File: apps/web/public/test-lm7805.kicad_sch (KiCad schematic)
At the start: 5 parts, among them J1 VIN_CONN, J2 VOUT_5V, U1 LM7805

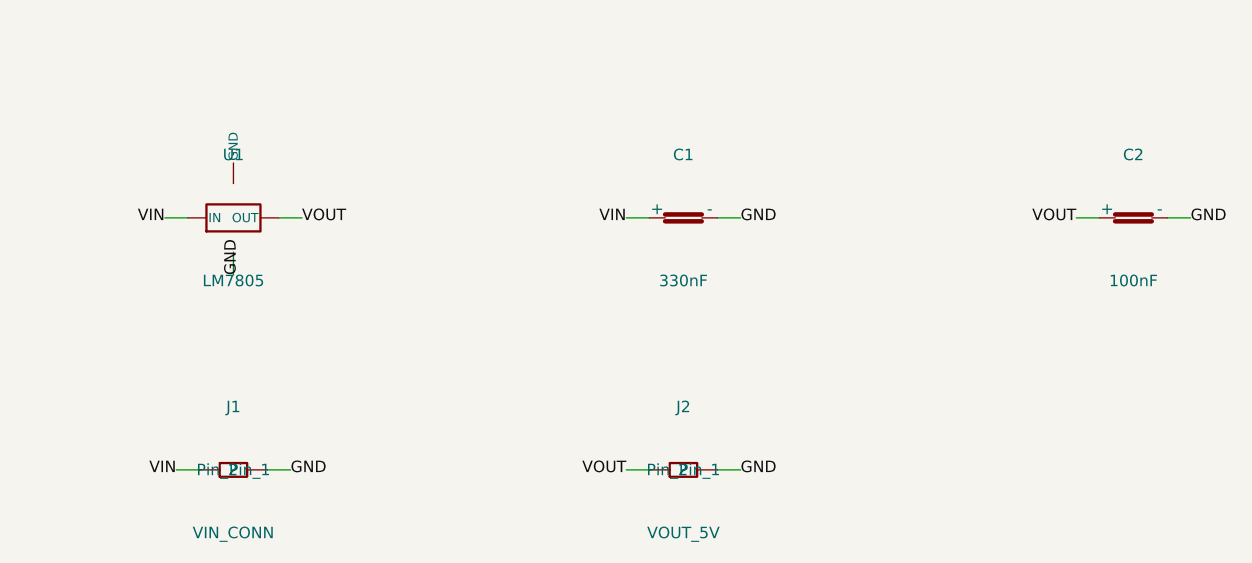
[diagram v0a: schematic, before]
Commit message: feat(kicad): Timer:NE555P named pins + compact paper for better zoom
- Add Timer:NE555P inline symbol with proper named pins:
  GND(1) TRIG(2) OUT(3) RST(4) CTRL(5) THR(6) DIS(7) VCC(8)
- _simple_lib_id: detect NE555/LM555/NA555/TLC555/ICM7555 → Timer:NE555P
- _pin_offset: Timer:NE555P reuses DIP-8 _IC_PIN_OFFSETS geometry
- Reduce paper margins 20→8mm, col_step 50→45, row_step 28→25
  LM7805 paper: 165x88 → 128x59mm (-40%) = composants 40% plus grands
  au zoom-to-fit KiCanvas
- Regenerate 3 fixtures (lm7805/ne555/esp32)
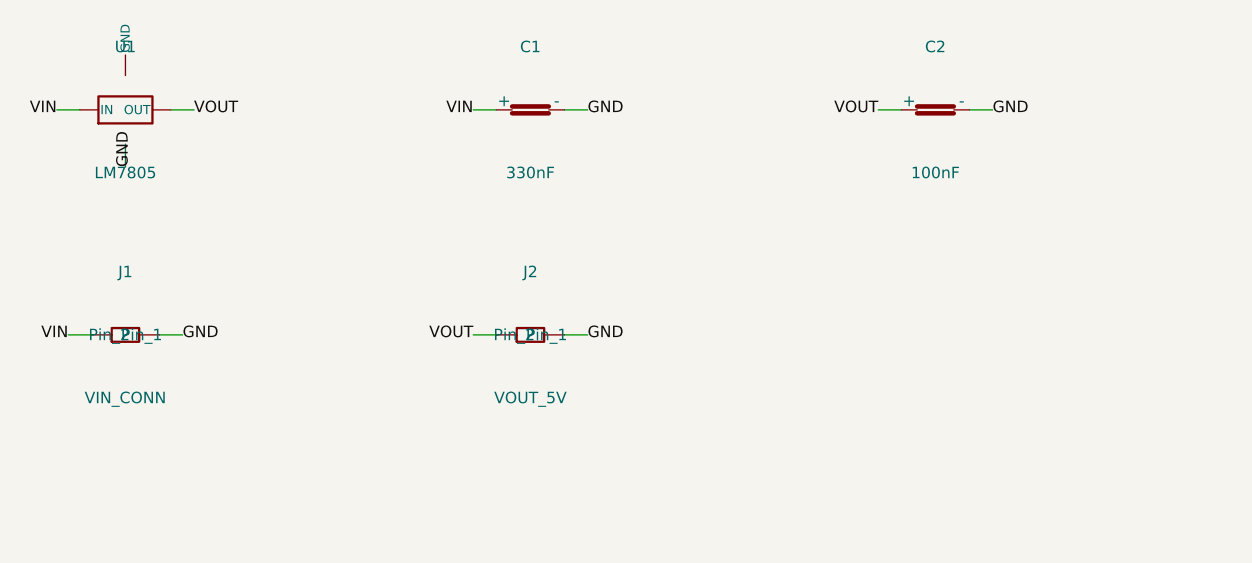
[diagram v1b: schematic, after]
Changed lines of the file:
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@@
 (kicad_sch (version 20230121) (generator "layrix-circuit-synth")
-  (paper "User" 165 88)
-  (symbol (lib_id "Device:VReg_3Pin") (at 20 20 0) (unit 1) (in_bom yes) (on_board yes)
-    (property "Reference" "U1" (at 20 13 0) (effects (font (size 1.27 1.27)) (justify center)))
-    (property "Value" "LM7805" (at 20 27 0) (effects (font (size 1.27 1.27)) (justify center)))
-    (property "Footprint" "Package_TO_SOT_THT:TO-220-3_Vertical" (at 20 30 0) (effects (font (size 1.27 1.27)) (hide yes)))
+  (paper "User" 128 59)
+  (symbol (lib_id "Device:VReg_3Pin") (at 8 8 0) (unit 1) (in_bom yes) (on_board yes)
+    (property "Reference" "U1" (at 8 1 0) (effects (font (size 1.27 1.27)) (justify center)))
+    (property "Value" "LM7805" (at 8 15 0) (effects (font (size 1.27 1.27)) (justify center)))
+    (property "Footprint" "Package_TO_SOT_THT:TO-220-3_Vertical" (at 8 18 0) (effects (font (size 1.27 1.27)) (hide yes)))
   )
-  (symbol (lib_id "Device:C") (at 70 20 0) (unit 1) (in_bom yes) (on_board yes)
-    (property "Reference" "C1" (at 70 13 0) (effects (font (size 1.27 1.27)) (justify center)))
-    (property "Value" "330nF" (at 70 27 0) (effects (font (size 1.27 1.27)) (justify center)))
-    (property "Footprint" "Capacitor_THT:C_Disc_D5.0mm_W2.5mm_P5.00mm" (at 70 30 0) (effects (font (size 1.27 1.27)) (hide yes)))
+  (symbol (lib_id "Device:C") (at 53 8 0) (unit 1) (in_bom yes) (on_board yes)
+    (property "Reference" "C1" (at 53 1 0) (effects (font (size 1.27 1.27)) (justify center)))
+    (property "Value" "330nF" (at 53 15 0) (effects (font (size 1.27 1.27)) (justify center)))
+    (property "Footprint" "Capacitor_THT:C_Disc_D5.0mm_W2.5mm_P5.00mm" (at 53 18 0) (effects (font (size 1.27 1.27)) (hide yes)))
   )
-  (symbol (lib_id "Device:C") (at 120 20 0) (unit 1) (in_bom yes) (on_board yes)
-    (property "Reference" "C2" (at 120 13 0) (effects (font (size 1.27 1.27)) (justify center)))
-    (property "Value" "100nF" (at 120 27 0) (effects (font (size 1.27 1.27)) (justify center)))
-    (property "Footprint" "Capacitor_THT:C_Disc_D5.0mm_W2.5mm_P5.00mm" (at 120 30 0) (effects (font (size 1.27 1.27)) (hide yes)))
+  (symbol (lib_id "Device:C") (at 98 8 0) (unit 1) (in_bom yes) (on_board yes)
+    (property "Reference" "C2" (at 98 1 0) (effects (font (size 1.27 1.27)) (justify center)))
+    (property "Value" "100nF" (at 98 15 0) (effects (font (size 1.27 1.27)) (justify center)))
+    (property "Footprint" "Capacitor_THT:C_Disc_D5.0mm_W2.5mm_P5.00mm" (at 98 18 0) (effects (font (size 1.27 1.27)) (hide yes)))
   )
-  (symbol (lib_id "Connector_Generic:Conn_01x02") (at 20 48 0) (unit 1) (in_bom yes) (on_board yes)
-    (property "Reference" "J1" (at 20 41 0) (effects (font (size 1.27 1.27)) (justify center)))
-    (property "Value" "VIN_CONN" (at 20 55 0) (effects (font (size 1.27 1.27)) (justify center)))
-    (property "Footprint" "Connector_PinHeader_2.54mm:PinHeader_1x02_P2.54mm_Vertical" (at 20 58 0) (effects (font (size 1.27 1.27)) (hide yes)))
+  (symbol (lib_id "Connector_Generic:Conn_01x02") (at 8 33 0) (unit 1) (in_bom yes) (on_board yes)
+    (property "Reference" "J1" (at 8 26 0) (effects (font (size 1.27 1.27)) (justify center)))
+    (property "Value" "VIN_CONN" (at 8 40 0) (effects (font (size 1.27 1.27)) (justify center)))
+    (property "Footprint" "Connector_PinHeader_2.54mm:PinHeader_1x02_P2.54mm_Vertical" (at 8 43 0) (effects (font (size 1.27 1.27)) (hide yes)))
   )
-  (symbol (lib_id "Connector_Generic:Conn_01x02") (at 70 48 0) (unit 1) (in_bom yes) (on_board yes)
-    (property "Reference" "J2" (at 70 41 0) (effects (font (size 1.27 1.27)) (justify center)))
-    (property "Value" "VOUT_5V" (at 70 55 0) (effects (font (size 1.27 1.27)) (justify center)))
-    (property "Footprint" "Connector_PinHeader_2.54mm:PinHeader_1x02_P2.54mm_Vertical" (at 70 58 0) (effects (font (size 1.27 1.27)) (hide yes)))
+  (symbol (lib_id "Connector_Generic:Conn_01x02") (at 53 33 0) (unit 1) (in_bom yes) (on_board yes)
+    (property "Reference" "J2" (at 53 26 0) (effects (font (size 1.27 1.27)) (justify center)))
+    (property "Value" "VOUT_5V" (at 53 40 0) (effects (font (size 1.27 1.27)) (justify center)))
+    (property "Footprint" "Connector_PinHeader_2.54mm:PinHeader_1x02_P2.54mm_Vertical" (at 53 43 0) (effects (font (size 1.27 1.27)) (hide yes)))
   )
-  (wire (pts (xy 14.92 20.0) (xy 12.38 20.0)) (stroke (width 0.1524) (type default)))
-  (label "VIN" (at 12.38 20.0 180) (effects (font (size 1.27 1.27))))
-  (wire (pts (xy 66.19 20.0) (xy 63.65 20.0)) (stroke (width 0.1524) (type default)))
-  (label "VIN" (at 63.65 20.0 180) (effects (font (size 1.27 1.27))))
-  (wire (pts (xy 16.19 48.0) (xy 13.65 48.0)) (stroke (width 0.1524) (type default)))
-  (label "VIN" (at 13.65 48.0 180) (effects (font (size 1.27 1.27))))
-  (wire (pts (xy 20.0 23.81) (xy 20.0 26.35)) (stroke (width 0.1524) (type default)))
-  (label "GND" (at 20.0 26.35 90) (effects (font (size 1.27 1.27))))
-  (wire (pts (xy 73.81 20.0) (xy 76.35 20.0)) (stroke (width 0.1524) (type default)))
-  (label "GND" (at 76.35 20.0 0) (effects (font (size 1.27 1.27))))
-  (wire (pts (xy 123.81 20.0) (xy 126.35 20.0)) (stroke (width 0.1524) (type default)))
-  (label "GND" (at 126.35 20.0 0) (effects (font (size 1.27 1.27))))
-  (wire (pts (xy 23.81 48.0) (xy 26.35 48.0)) (stroke (width 0.1524) (type default)))
-  (label "GND" (at 26.35 48.0 0) (effects (font (size 1.27 1.27))))
-  (wire (pts (xy 73.81 48.0) (xy 76.35 48.0)) (stroke (width 0.1524) (type default)))
-  (label "GND" (at 76.35 48.0 0) (effects (font (size 1.27 1.27))))
-  (wire (pts (xy 25.08 20.0) (xy 27.62 20.0)) (stroke (width 0.1524) (type default)))
-  (label "VOUT" (at 27.62 20.0 0) (effects (font (size 1.27 1.27))))
-  (wire (pts (xy 116.19 20.0) (xy 113.65 20.0)) (stroke (width 0.1524) (type default)))
-  (label "VOUT" (at 113.65 20.0 180) (effects (font (size 1.27 1.27))))
-  (wire (pts (xy 66.19 48.0) (xy 63.65 48.0)) (stroke (width 0.1524) (type default)))
-  (label "VOUT" (at 63.65 48.0 180) (effects (font (size 1.27 1.27))))
+  (wire (pts (xy 2.92 8.0) (xy 0.38 8.0)) (stroke (width 0.1524) (type default)))
+  (label "VIN" (at 0.38 8.0 180) (effects (font (size 1.27 1.27))))
+  (wire (pts (xy 49.19 8.0) (xy 46.65 8.0)) (stroke (width 0.1524) (type default)))
+  (label "VIN" (at 46.65 8.0 180) (effects (font (size 1.27 1.27))))
+  (wire (pts (xy 4.19 33.0) (xy 1.65 33.0)) (stroke (width 0.1524) (type default)))
+  (label "VIN" (at 1.65 33.0 180) (effects (font (size 1.27 1.27))))
+  (wire (pts (xy 8.0 11.81) (xy 8.0 14.35)) (stroke (width 0.1524) (type default)))
+  (label "GND" (at 8.0 14.35 90) (effects (font (size 1.27 1.27))))
+  (wire (pts (xy 56.81 8.0) (xy 59.35 8.0)) (stroke (width 0.1524) (type default)))
+  (label "GND" (at 59.35 8.0 0) (effects (font (size 1.27 1.27))))
+  (wire (pts (xy 101.81 8.0) (xy 104.35 8.0)) (stroke (width 0.1524) (type default)))
+  (label "GND" (at 104.35 8.0 0) (effects (font (size 1.27 1.27))))
+  (wire (pts (xy 11.81 33.0) (xy 14.35 33.0)) (stroke (width 0.1524) (type default)))
+  (label "GND" (at 14.35 33.0 0) (effects (font (size 1.27 1.27))))
+  (wire (pts (xy 56.81 33.0) (xy 59.35 33.0)) (stroke (width 0.1524) (type default)))
+  (label "GND" (at 59.35 33.0 0) (effects (font (size 1.27 1.27))))
+  (wire (pts (xy 13.08 8.0) (xy 15.62 8.0)) (stroke (width 0.1524) (type default)))
+  (label "VOUT" (at 15.62 8.0 0) (effects (font (size 1.27 1.27))))
+  (wire (pts (xy 94.19 8.0) (xy 91.65 8.0)) (stroke (width 0.1524) (type default)))
+  (label "VOUT" (at 91.65 8.0 180) (effects (font (size 1.27 1.27))))
+  (wire (pts (xy 49.19 33.0) (xy 46.65 33.0)) (stroke (width 0.1524) (type default)))
+  (label "VOUT" (at 46.65 33.0 180) (effects (font (size 1.27 1.27))))
   (sheet_instances (path "/" (page "1")))
 )
